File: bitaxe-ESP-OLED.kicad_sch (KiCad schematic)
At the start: 61 parts, among them J1 Conn_01x06, J2 USB_C_Receptacle_USB2.0_16P, J3 TC2030-IDC, J4 SFV30R-4STE1HLF, Q1 SI2307, SW1 SWITCH-SPST, SW2 SWITCH-SPST, SW3 SWITCH-SPST, SW4 SWITCH-SPST, U1 RT9080-33GJ5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

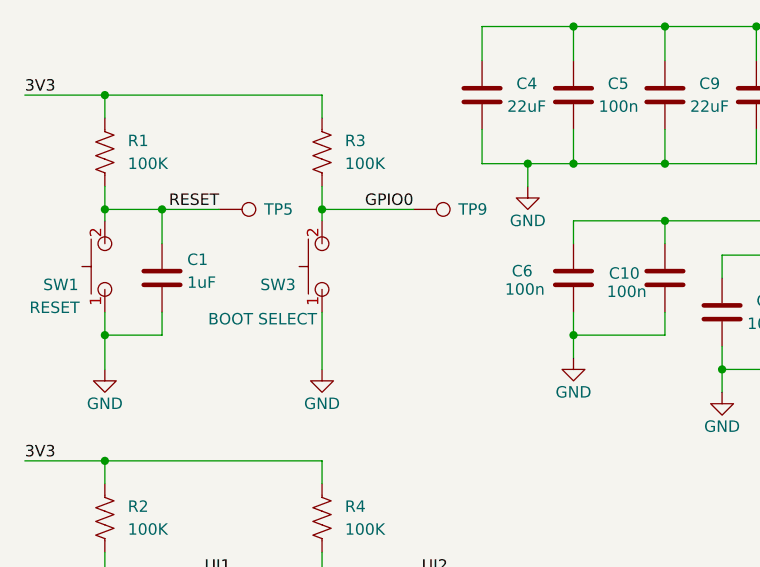
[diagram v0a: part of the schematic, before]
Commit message: moved switches
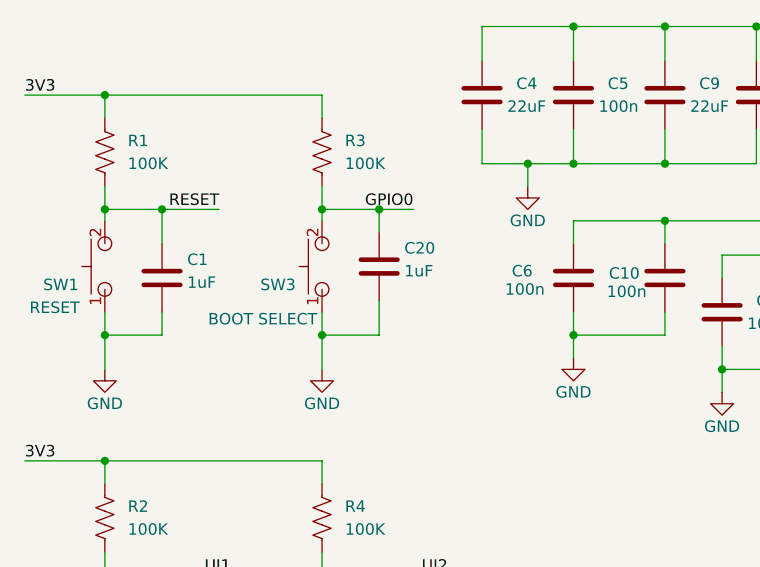
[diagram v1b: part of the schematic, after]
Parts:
- removed TP5, TP9: TestPoint, TestPoint:TestPoint_Pad_D1.0mm, symbol Connector:TestPoint
- added C20: 1uF, Capacitor_SMD:C_0402_1005Metric, symbol Device:C
- C2, C3: PARTNO EMK105BJ105MV-F -> TL3340AF160QG
- SW2, SW4: DK 141-TL3301NF160QG-KRCT-ND -> EG4627CT-ND
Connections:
- net GND: now also C20.2
- net GPIO0: now also C20.1
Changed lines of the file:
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@@
 	)
 	(junction
+		(at 55.88 35.56)
+		(diameter 0)
+		(color 0 0 0 0)
+	)
+	(junction
 		(at 77.47 15.24)
 		(diameter 0)
@@
 	)
 	(junction
+		(at 49.53 49.53)
+		(diameter 0)
+		(color 0 0 0 0)
+	)
+	(junction
 		(at 77.47 30.48)
 		(diameter 0)
@@
 	(wire
 		(pts
+			(xy 49.53 49.53) (xy 49.53 53.34)
+		)
+		(stroke
+			(width 0)
+			(type default)
+		)
+	)
+	(wire
+		(pts
 			(xy 29.21 186.69) (xy 36.83 186.69)
 		)
@@
 	(wire
 		(pts
-			(xy 49.53 35.56) (xy 59.69 35.56)
+			(xy 49.53 35.56) (xy 55.88 35.56)
 		)
 		(stroke
@@
 	(wire
 		(pts
-			(xy 49.53 46.99) (xy 49.53 53.34)
+			(xy 49.53 46.99) (xy 49.53 49.53)
 		)
 		(stroke
@@
 	(wire
 		(pts
+			(xy 55.88 35.56) (xy 55.88 38.1)
+		)
+		(stroke
+			(width 0)
+			(type default)
+		)
+	)
+	(wire
+		(pts
 			(xy 128.27 33.02) (xy 133.35 33.02)
 		)
@@
 	(wire
 		(pts
+			(xy 55.88 35.56) (xy 59.69 35.56)
+		)
+		(stroke
+			(width 0)
+			(type default)
+		)
+	)
+	(wire
+		(pts
 			(xy 93.98 53.34) (xy 93.98 50.8)
 		)
@@
 	(wire
 		(pts
+			(xy 55.88 49.53) (xy 49.53 49.53)
+		)
+		(stroke
+			(width 0)
+			(type default)
+		)
+	)
+	(wire
+		(pts
 			(xy 86.36 95.25) (xy 95.25 95.25)
 		)
@@
 	(wire
 		(pts
+			(xy 55.88 45.72) (xy 55.88 49.53)
+		)
+		(stroke
+			(width 0)
+			(type default)
+		)
+	)
+	(wire
+		(pts
 			(xy 146.05 166.37) (xy 135.89 166.37)
 		)
@@
 			)
 		)
-		(property "PARTNO" "EMK105BJ105MV-F"
+		(property "PARTNO" "TL3340AF160QG"
 			(at 31.75 83.82 0)
 			(effects
@@
 	)
 	(symbol
-		(lib_id "Connector:TestPoint")
-		(at 59.69 35.56 270)
-		(unit 1)
-		(exclude_from_sim no)
-		(in_bom yes)
-		(on_board yes)
-		(dnp no)
-		(property "Reference" "TP9"
-			(at 66.294 35.56 90)
-			(effects
-				(font
-					(size 1.27 1.27)
-				)
-			)
-		)
-		(property "Value" "TestPoint"
-			(at 62.992 38.1 90)
-			(effects
-				(font
-					(size 1.27 1.27)
-				)
-				(hide yes)
-			)
-		)
-		(property "Footprint" "TestPoint:TestPoint_Pad_D1.0mm"
-			(at 59.69 40.64 0)
-			(effects
-				(font
-					(size 1.27 1.27)
-				)
-				(hide yes)
-			)
-		)
-		(property "Datasheet" "~"
-			(at 59.69 40.64 0)
-			(effects
-				(font
-					(size 1.27 1.27)
-				)
-				(hide yes)
-			)
-		)
-		(property "Description" "test point"
-			(at 59.69 35.56 0)
-			(effects
-				(font
-					(size 1.27 1.27)
-				)
-				(hide yes)
-			)
-		)
-		(pin "1"
-		)
-		(instances
-			(project "bitaxe-ESP-OLED"
-				(path "/4620448a-8f8c-4f0c-a7dd-d620330051ff"
-					(reference "TP9")
-					(unit 1)
-				)
-			)
-		)
-	)
-	(symbol
 		(lib_id "Device:C")
 		(at 67.31 22.86 0)
@@
 	)
 	(symbol
-		(lib_id "Connector:TestPoint")
-		(at 38.1 35.56 270)
-		(unit 1)
-		(exclude_from_sim no)
-		(in_bom yes)
-		(on_board yes)
-		(dnp no)
-		(property "Reference" "TP5"
-			(at 44.704 35.56 90)
-			(effects
-				(font
-					(size 1.27 1.27)
-				)
-			)
-		)
-		(property "Value" "TestPoint"
-			(at 41.402 38.1 90)
-			(effects
-				(font
-					(size 1.27 1.27)
-				)
-				(hide yes)
-			)
-		)
-		(property "Footprint" "TestPoint:TestPoint_Pad_D1.0mm"
-			(at 38.1 40.64 0)
-			(effects
-				(font
-					(size 1.27 1.27)
-				)
-				(hide yes)
-			)
-		)
-		(property "Datasheet" "~"
-			(at 38.1 40.64 0)
-			(effects
-				(font
-					(size 1.27 1.27)
-				)
-				(hide yes)
-			)
-		)
-		(property "Description" "test point"
-			(at 38.1 35.56 0)
-			(effects
-				(font
-					(size 1.27 1.27)
-				)
-				(hide yes)
-			)
-		)
-		(pin "1"
-		)
-		(instances
-			(project "bitaxe-ESP-OLED"
-				(path "/4620448a-8f8c-4f0c-a7dd-d620330051ff"
-					(reference "TP5")
-					(unit 1)
-				)
-			)
-		)
-	)
-	(symbol
 		(lib_id "Device:C")
 		(at 55.88 83.82 0)
@@
 			)
 		)
-		(property "PARTNO" "EMK105BJ105MV-F"
+		(property "PARTNO" "TL3340AF160QG"
 			(at 55.88 83.82 0)
 			(effects
@@
 	)
 	(symbol
+		(lib_id "Device:C")
+		(at 55.88 41.91 0)
+		(unit 1)
+		(exclude_from_sim no)
+		(in_bom yes)
+		(on_board yes)
+		(dnp no)
+		(property "Reference" "C20"
+			(at 58.674 39.878 0)
+			(effects
+				(font
+					(size 1.27 1.27)
+				)
+				(justify left)
+			)
+		)
+		(property "Value" "1uF"
+			(at 58.674 42.418 0)
+			(effects
+				(font
+					(size 1.27 1.27)
+				)
+				(justify left)
+			)
+		)
+		(property "Footprint" "Capacitor_SMD:C_0402_1005Metric"
+			(at 56.8452 45.72 0)
+			(effects
+				(font
+					(size 1.27 1.27)
+				)
+				(hide yes)
+			)
+		)
+		(property "Datasheet" "~"
+			(at 55.88 41.91 0)
+			(effects
+				(font
+					(size 1.27 1.27)
+				)
+				(hide yes)
+			)
+		)
+		(property "Description" "Unpolarized capacitor"
+			(at 55.88 41.91 0)
+			(effects
+				(font
+					(size 1.27 1.27)
+				)
+				(hide yes)
+			)
+		)
+		(property "PARTNO" "TL3340AF160QG"
+			(at 55.88 41.91 0)
+			(effects
+				(font
+					(size 1.27 1.27)
+				)
+				(hide yes)
+			)
+		)
+		(property "DK" "587-5514-1-ND"
+			(at 55.88 41.91 0)
+			(effects
+				(font
+					(size 1.27 1.27)
+				)
+				(hide yes)
+			)
+		)
+		(pin "1"
+		)
+		(pin "2"
+		)
+		(instances
+			(project "bitaxe-ESP-OLED"
+				(path "/4620448a-8f8c-4f0c-a7dd-d620330051ff"
+					(reference "C20")
+					(unit 1)
+				)
+			)
+		)
+	)
+	(symbol
 		(lib_id "power:GND")
 		(at 125.73 181.61 0)
@@
 			)
 		)
-		(property "Datasheet" "https://eswitch.wpengine.com/wp-content/uploads/2022/06/TL3301-1.pdf"
+		(property "Datasheet" "https://sten-eswitch-13110800-production.s3.amazonaws.com/system/asset/product_line/data_sheet/164/TL3340.pdf"
 			(at 59.69 82.55 0)
 			(effects
@@
 			)
 		)
-		(property "Description" "SMD SPST button"
+		(property "Description" "SMD right-angle SPST button"
 			(at 49.53 82.55 0)
 			(effects
@@
 			)
 		)
-		(property "DK" "141-TL3301NF160QG-KRCT-ND"
+		(property "DK" "EG4627CT-ND"
 			(at 50.8 82.55 0)
 			(effects
@@
 			)
 		)
-		(property "Datasheet" "https://eswitch.wpengine.com/wp-content/uploads/2022/06/TL3301-1.pdf"
+		(property "Datasheet" "https://sten-eswitch-13110800-production.s3.amazonaws.com/system/asset/product_line/data_sheet/164/TL3340.pdf"
 			(at 35.56 82.55 0)
 			(effects
@@
 			)
 		)
-		(property "Description" "SMD SPST button"
+		(property "Description" "SMD right-angle SPST button"
 			(at 25.4 82.55 0)
 			(effects
@@
 			)
 		)
-		(property "DK" "141-TL3301NF160QG-KRCT-ND"
+		(property "DK" "EG4627CT-ND"
 			(at 26.67 82.55 0)
 			(effects

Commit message: v0.3
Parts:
- removed H1, H2: MountingHole, MountingHole:MountingHole_3mm_Pad_Via, symbol Mechanical:MountingHole
- J1: footprint Connector_PinHeader_2.54mm:PinHeader_1x06_P2.54mm_Vertical -> Connector_PinSocket_1.27mm:PinSocket_2x03_P1.27mm_Vertical_SMD
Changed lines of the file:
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@@
 			)
 		)
-		(property "Footprint" "Connector_PinHeader_2.54mm:PinHeader_1x06_P2.54mm_Vertical"
+		(property "Footprint" "Connector_PinSocket_1.27mm:PinSocket_2x03_P1.27mm_Vertical_SMD"
 			(at 25.4 120.65 0)
 			(effects
@@
 	)
 	(symbol
-		(lib_id "Mechanical:MountingHole")
-		(at 241.3 160.02 0)
-		(unit 1)
-		(exclude_from_sim no)
-		(in_bom yes)
-		(on_board yes)
-		(dnp no)
-		(fields_autoplaced yes)
-		(property "Reference" "H2"
-			(at 243.84 158.7499 0)
-			(effects
-				(font
-					(size 1.27 1.27)
-				)
-				(justify left)
-			)
-		)
-		(property "Value" "MountingHole"
-			(at 243.84 161.2899 0)
-			(effects
-				(font
-					(size 1.27 1.27)
-				)
-				(justify left)
-			)
-		)
-		(property "Footprint" "MountingHole:MountingHole_3mm_Pad_Via"
-			(at 241.3 160.02 0)
-			(effects
-				(font
-					(size 1.27 1.27)
-				)
-				(hide yes)
-			)
-		)
-		(property "Datasheet" "~"
-			(at 241.3 160.02 0)
-			(effects
-				(font
-					(size 1.27 1.27)
-				)
-				(hide yes)
-			)
-		)
-		(property "Description" "Mounting Hole without connection"
-			(at 241.3 160.02 0)
-			(effects
-				(font
-					(size 1.27 1.27)
-				)
-				(hide yes)
-			)
-		)
-		(instances
-			(project "bitaxe-ESP-OLED"
-				(path "/4620448a-8f8c-4f0c-a7dd-d620330051ff"
-					(reference "H2")
-					(unit 1)
-				)
-			)
-		)
-	)
-	(symbol
 		(lib_id "Device:R_US")
 		(at 207.01 81.28 0)
@@
 					(unit 1)
 				)
-			)
-		)
-	)
-	(symbol
-		(lib_id "Mechanical:MountingHole")
-		(at 241.3 153.67 0)
-		(unit 1)
-		(exclude_from_sim no)
-		(in_bom yes)
-		(on_board yes)
-		(dnp no)
-		(fields_autoplaced yes)
-		(property "Reference" "H1"
-			(at 243.84 152.3999 0)
-			(effects
-				(font
-					(size 1.27 1.27)
-				)
-				(justify left)
-			)
-		)
-		(property "Value" "MountingHole"
-			(at 243.84 154.9399 0)
-			(effects
-				(font
-					(size 1.27 1.27)
-				)
-				(justify left)
-			)
-		)
-		(property "Footprint" "MountingHole:MountingHole_3mm_Pad_Via"
-			(at 241.3 153.67 0)
-			(effects
-				(font
-					(size 1.27 1.27)
-				)
-				(hide yes)
-			)
-		)
-		(property "Datasheet" "~"
-			(at 241.3 153.67 0)
-			(effects
-				(font
-					(size 1.27 1.27)
-				)
-				(hide yes)
-			)
-		)
-		(property "Description" "Mounting Hole without connection"
-			(at 241.3 153.67 0)
-			(effects
-				(font
-					(size 1.27 1.27)
-				)
-				(hide yes)
-			)
-		)
-		(instances
-			(project "bitaxe-ESP-OLED"
-				(path "/4620448a-8f8c-4f0c-a7dd-d620330051ff"
-					(reference "H1")
-					(unit 1)
-				)

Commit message: Expand copper pour underneath MCU
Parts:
- U3: footprint Package_TO_SOT_SMD:SOT-23-6 -> bitaxe:SOT-23-6
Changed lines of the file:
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@@
 	(title_block
 		(title "Bitaxe ESP-OLED")
-		(rev "0.1")
+		(date "2024-11-01")
+		(rev "0.4")
 	)
 	(junction
@@
 			)
 		)
-		(property "Footprint" "Package_TO_SOT_SMD:SOT-23-6"
+		(property "Footprint" "bitaxe:SOT-23-6"
 			(at 198.12 114.3 0)
 			(effects
